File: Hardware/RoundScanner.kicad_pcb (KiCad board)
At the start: 4 copper layers, 45 x 42.5 mm, 82 parts, among them J1 I2C ThroughHole, J3 I2C, J4 Interface, Q1 BSS138DW-7-F, U1 OPA2376xxD, U2 NAU7802SGI, U4 OPA2376xxD, U5 TLC59208FIPWR, U6 AS7341-DLGT, U7 AP7312-1833W6-7, X1 SG-8002CE

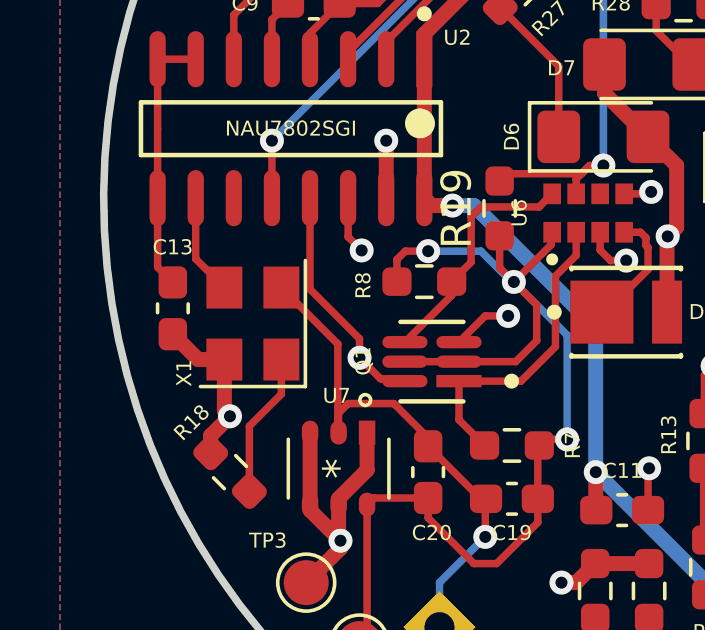
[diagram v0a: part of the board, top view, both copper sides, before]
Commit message: added recommended crystal layout to board
Signed-off-by: lokimetasmith <lokimail@gmail.com>
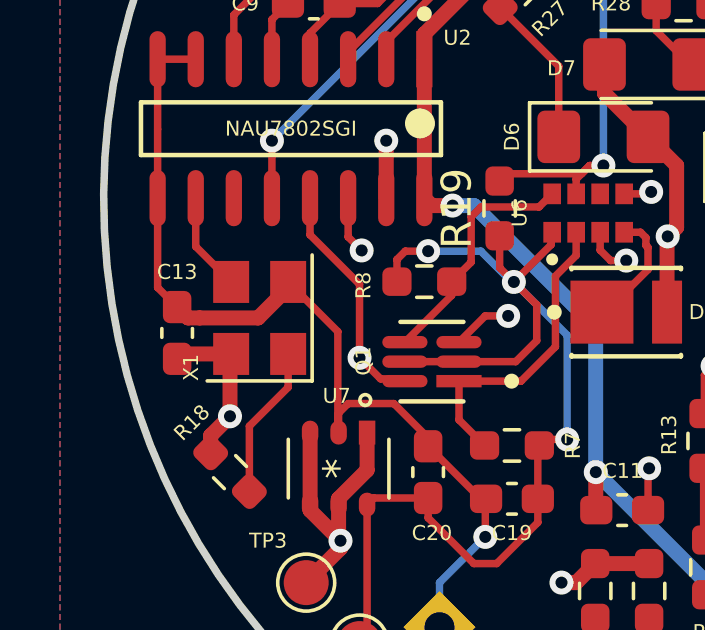
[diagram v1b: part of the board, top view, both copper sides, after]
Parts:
- moved C13 0.83 mm to (69.2, 111.8)
- moved X1 0.29 mm to (72.0, 111.3)
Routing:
- net GND: track 58.1 -> 63.8 mm
